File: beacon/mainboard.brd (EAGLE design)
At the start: 26.1 x 66.7 mm, 4 parts, among them J1 1X2-3.5MM

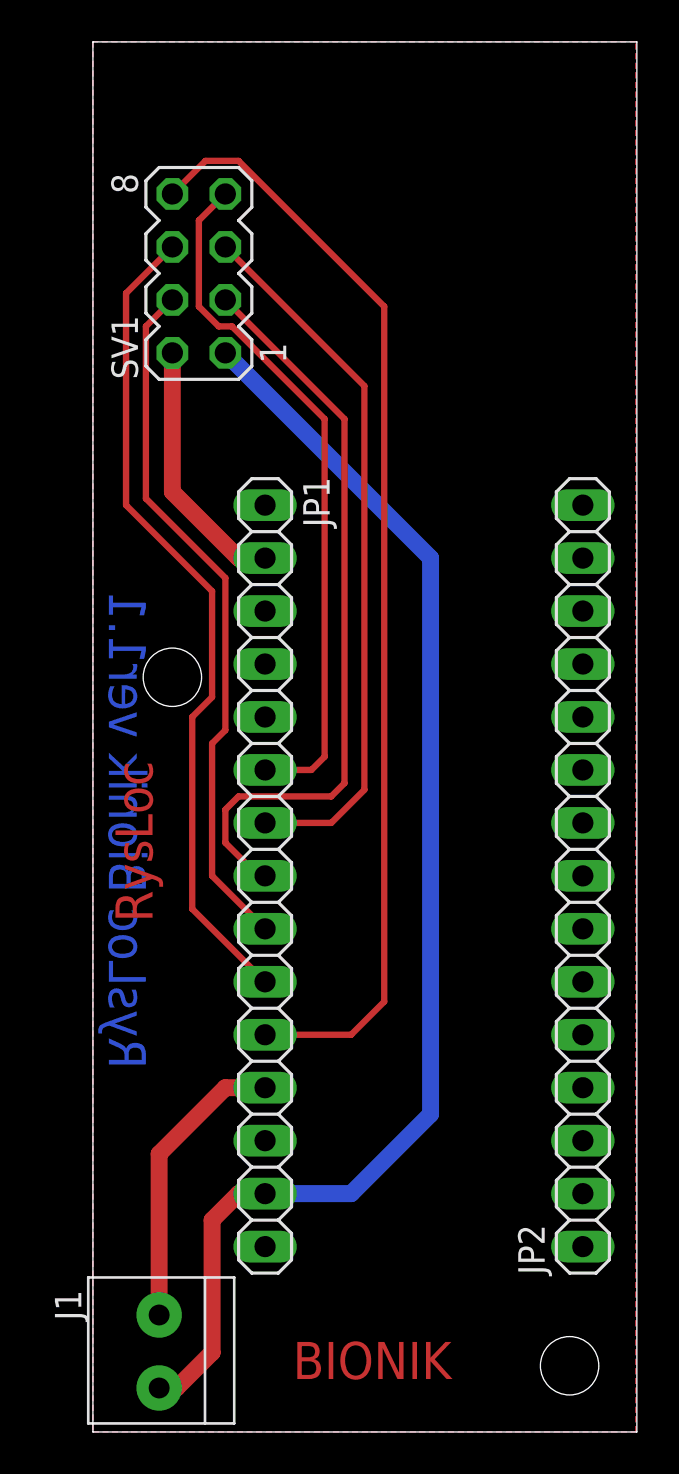
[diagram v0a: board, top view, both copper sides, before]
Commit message: latarnia (beacon): zmniejszone wymiary płytki
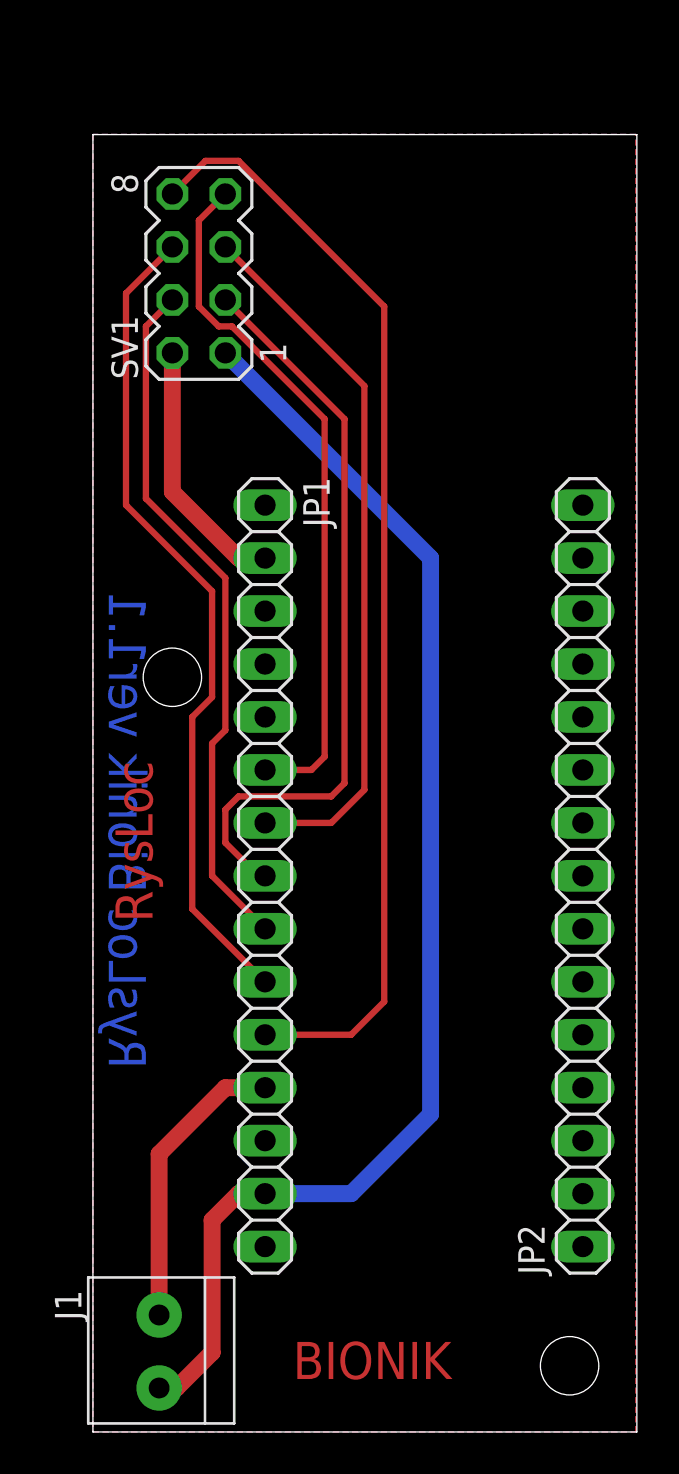
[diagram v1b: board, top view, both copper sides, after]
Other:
- board size 26.1 x 66.7 mm -> 26.1 x 62.2 mm
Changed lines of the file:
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@@
 <plain>
 <wire x1="67.945" y1="7.62" x2="94.031" y2="7.62" width="0" layer="20"/>
-<wire x1="94.031" y1="7.62" x2="94.031" y2="74.285" width="0" layer="20"/>
-<wire x1="94.031" y1="74.285" x2="67.945" y2="74.285" width="0" layer="20"/>
-<wire x1="67.945" y1="74.285" x2="67.945" y2="7.62" width="0" layer="20"/>
+<wire x1="94.031" y1="7.62" x2="94.031" y2="69.84" width="0" layer="20"/>
+<wire x1="94.031" y1="69.84" x2="67.945" y2="69.84" width="0" layer="20"/>
+<wire x1="67.945" y1="69.84" x2="67.945" y2="7.62" width="0" layer="20"/>
 <text x="70.485" y="47.9425" size="1.778" layer="16" rot="MR270">RysLoc Bionik ver1.1</text>
 <hole x="90.805" y="10.795" drill="2.8"/>
@@
 <signal name="GND">
 <contactref element="JP1" pad="14"/>
-<polygon width="0.3048" layer="1" isolate="0.3048">
-<vertex x="67.945" y="74.295"/>
+<polygon width="0.0762" layer="1" isolate="0.3048">
+<vertex x="67.945" y="69.85"/>
 <vertex x="67.945" y="7.62"/>
 <vertex x="93.98" y="7.62"/>
-<vertex x="93.98" y="74.295"/>
+<vertex x="93.98" y="69.85"/>
 </polygon>
-<polygon width="0.4064" layer="16" spacing="0.3048" isolate="0.3048">
-<vertex x="67.945" y="74.295"/>
+<polygon width="0.0762" layer="16" spacing="0.3048" isolate="0.3048">
+<vertex x="67.945" y="69.85"/>
 <vertex x="67.945" y="7.62"/>
 <vertex x="93.98" y="7.62"/>
-<vertex x="93.98" y="74.295"/>
+<vertex x="93.98" y="69.85"/>
 </polygon>
 <contactref element="J1" pad="2"/>
